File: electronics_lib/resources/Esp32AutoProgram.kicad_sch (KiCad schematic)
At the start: 4 parts

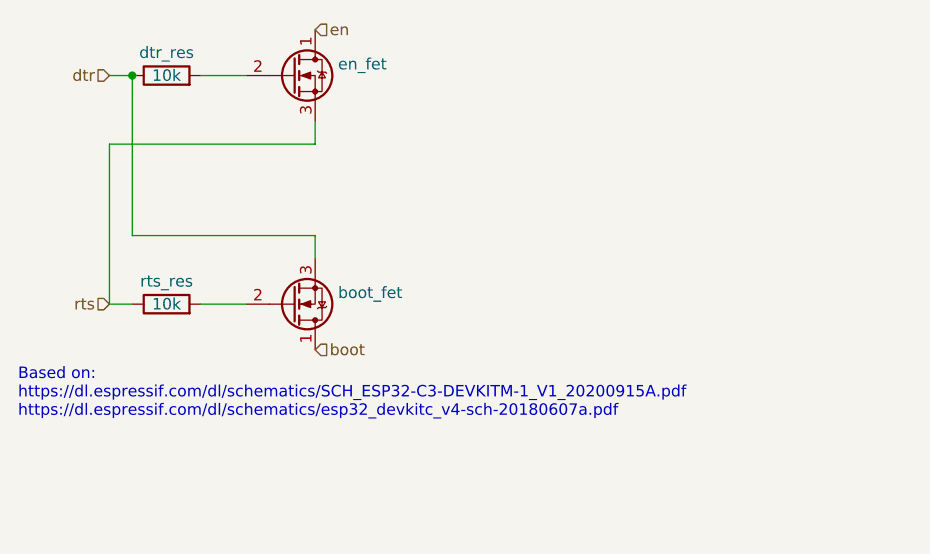
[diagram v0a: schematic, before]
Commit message: Update Esp32AutoProgram.kicad_sch
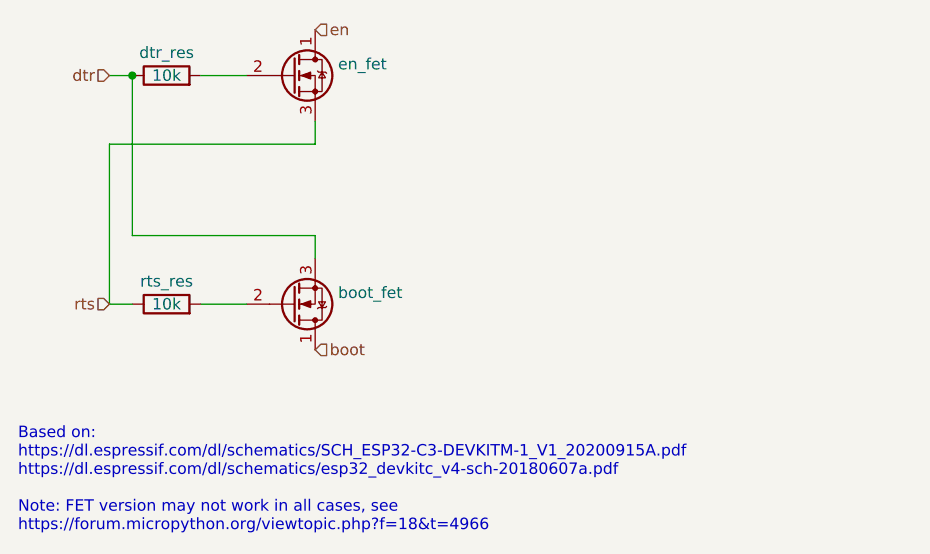
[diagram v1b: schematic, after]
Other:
- note added: "Based on: https://dl.espressif.com/dl/schematics/SCH_ESP32-C3-DEVKITM-1_V1_20200915A.pdf https://dl.espressif.com/dl/schematics/esp32_devkitc_v4-sch-20180607a.pdf Note: FET version may not work in all cases, see https://forum.micropython.org/viewtopic.php?f=18&t=4966"
- note removed: "Based on: https://dl.espressif.com/dl/schematics/SCH_ESP32-C3-DEVKITM-1_V1_20200915A.pdf https://dl.espressif.com/dl/schematics/esp32_devkitc_v4-sch-20180607a.pdf"
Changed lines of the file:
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@@
     (stroke (width 0) (type default) (color 0 0 0 0))
   )
-  (text "Based on:\nhttps://dl.espressif.com/dl/schematics/SCH_ESP32-C3-DEVKITM-1_V1_20200915A.pdf\nhttps://dl.espressif.com/dl/schematics/esp32_devkitc_v4-sch-20180607a.pdf"
-    (at 114.3 114.3 0)
+  (text "Based on:\nhttps://dl.espressif.com/dl/schematics/SCH_ESP32-C3-DEVKITM-1_V1_20200915A.pdf\nhttps://dl.espressif.com/dl/schematics/esp32_devkitc_v4-sch-20180607a.pdf\n\nNote: FET version may not work in all cases, see\nhttps://forum.micropython.org/viewtopic.php?f=18&t=4966"
+    (at 114.3 127 0)
     (effects (font (size 1.27 1.27)) (justify left bottom))
   )

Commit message: add bjts
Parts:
- removed boot_fet, en_fet: ~, symbol Device:Q_NMOS_DGS
- added q_boot, q_en: ~, symbol Device:Q_NPN_BCE
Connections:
- net boot: now also q_boot.2 (C)
- net dtr: now also q_boot.3 (E)
- net en: now also q_en.2 (C)
- net rts: now also q_en.3 (E)
- net at rts_res.2: now also q_boot.1 (B)
- net at dtr_res.2: now also q_en.1 (B)
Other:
- note added: "Based on: https://dl.espressif.com/dl/schematics/SCH_ESP32-C3-DEVKITM-1_V1_20200915A.pdf https://dl.espressif.com/dl/schematics/esp32_devkitc_v4-sch-20180607a.pdf"
- note removed: "Based on: https://dl.espressif.com/dl/schematics/SCH_ESP32-C3-DEVKITM-1_V1_20200915A.pdf https://dl.espressif.com/dl/schematics/esp32_devkitc_v4-sch-20180607a.pdf Note: FET version may not work in all cases, see https://forum.micropython.org/viewtopic.php?f=18&t=4966"
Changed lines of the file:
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@@
     (stroke (width 0) (type default) (color 0 0 0 0))
   )
-  (text "Based on:\nhttps://dl.espressif.com/dl/schematics/SCH_ESP32-C3-DEVKITM-1_V1_20200915A.pdf\nhttps://dl.espressif.com/dl/schematics/esp32_devkitc_v4-sch-20180607a.pdf\n\nNote: FET version may not work in all cases, see\nhttps://forum.micropython.org/viewtopic.php?f=18&t=4966"
-    (at 114.3 127 0)
+  (text "Based on:\nhttps://dl.espressif.com/dl/schematics/SCH_ESP32-C3-DEVKITM-1_V1_20200915A.pdf\nhttps://dl.espressif.com/dl/schematics/esp32_devkitc_v4-sch-20180607a.pdf"
+    (at 114.3 114.3 0)
     (effects (font (size 1.27 1.27)) (justify left bottom))
   )
@@
     (effects (font (size 1.27 1.27)) (justify right))
   )
-  (symbol (lib_id "Device:Q_NMOS_DGS") (at 144.78 101.6 0) (mirror x) (unit 1)
-    (in_bom yes) (on_board yes)
-    (property "Reference" "boot_fet" (id 0) (at 149.86 100.33 0)
+  (symbol (lib_name "Q_NPN_BCE_1") (lib_id "Device:Q_NPN_BCE") (at 144.78 101.6 0) (mirror x) (unit 1)
+    (in_bom yes) (on_board yes) (fields_autoplaced)
+    (property "Reference" "q_boot" (id 0) (at 149.86 100.3299 0)
       (effects (font (size 1.27 1.27)) (justify left))
     )
-    (property "Value" "~" (id 1) (at 151.13 102.8699 0)
+    (property "Value" "~" (id 1) (at 149.86 102.8699 0)
       (effects (font (size 1.27 1.27)) (justify left))
     )
@@
     (pin "2")
   )
-  (symbol (lib_id "Device:Q_NMOS_DGS") (at 144.78 76.2 0) (unit 1)
-    (in_bom yes) (on_board yes)
-    (property "Reference" "en_fet" (id 0) (at 149.86 74.93 0)
+  (symbol (lib_id "Device:Q_NPN_BCE") (at 144.78 76.2 0) (unit 1)
+    (in_bom yes) (on_board yes) (fields_autoplaced)
+    (property "Reference" "q_en" (id 0) (at 149.86 74.9299 0)
       (effects (font (size 1.27 1.27)) (justify left))
     )
-    (property "Value" "~" (id 1) (at 151.13 77.4699 0)
+    (property "Value" "~" (id 1) (at 149.86 77.4699 0)
       (effects (font (size 1.27 1.27)) (justify left))
     )
@@
   )
   (symbol_instances
-    (path "/3decfe3e-926e-45e0-b59f-5db47108adeb"
-      (reference "boot_fet") (unit 1) (value "~") (footprint "")
-    )
     (path "/69f754fc-9a05-49b5-92d4-e73f3379b1c3"
       (reference "dtr_res") (unit 1) (value "10k") (footprint "")
     )
-    (path "/d0318a72-4864-4360-b8a3-ff360ff90c64"
-      (reference "en_fet") (unit 1) (value "~") (footprint "")
+    (path "/526321e0-9da3-4190-8575-2f059700b6f2"
+      (reference "q_boot") (unit 1) (value "~") (footprint "")
+    )
+    (path "/c2ba90fb-a696-464c-b282-86d8f8eee0f5"
+      (reference "q_en") (unit 1) (value "~") (footprint "")
     )
     (path "/8652828a-fbde-461c-8a48-72b9b78993c2"
